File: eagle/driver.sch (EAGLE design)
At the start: 89 parts, among them IC1 XMEGA128A1, IC10 ST95P08M, IC11 ST95P08M, IC12 ST95P08M, IC13 ST95P08M, IC14 ST95P08M, IC15 ST95P08M, IC16 74AHC1G02DBV, IC17 74AHC1G02DBV, IC18 74AHC1G125DBV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

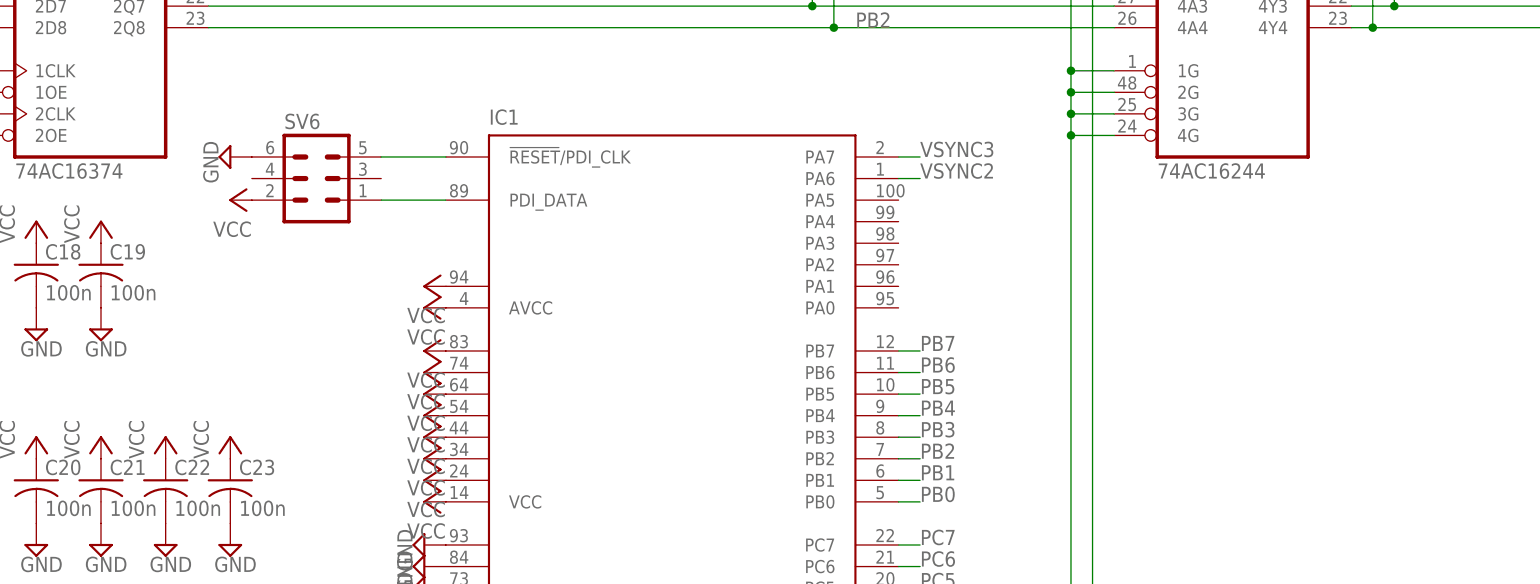
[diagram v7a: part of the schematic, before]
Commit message: add reset button and status leds
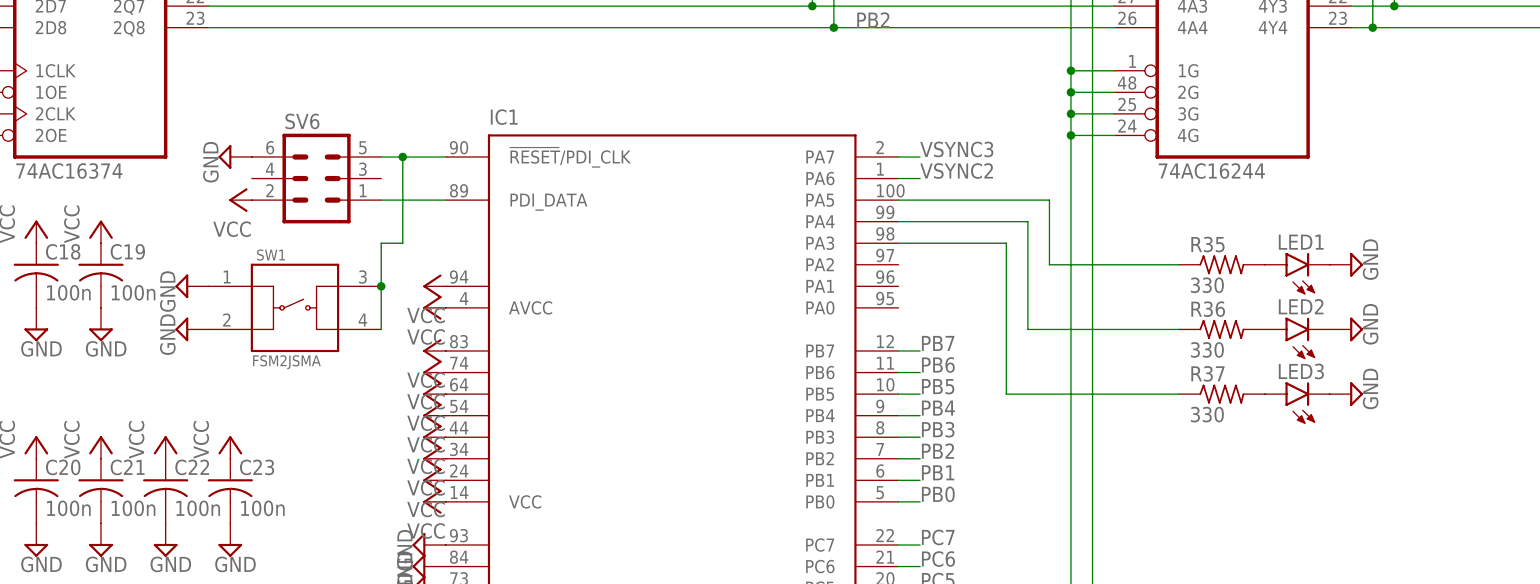
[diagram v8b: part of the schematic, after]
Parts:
- added LED1, LED2, LED3: (no value), led:LEDCHIPLED_0805
- added R35, R36, R37: 330, rcl:R-US_R0402
- added SW1: FSM2JSMA, Switch:FSM2JSMA
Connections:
- removed net N$88: IC1.!RESET!/PDI_CLK, SV6.5
- new net N$63: IC1.!RESET!/PDI_CLK, SV6.5, SW1.3, SW1.4
- new net N$66: LED3.A, R37.2
- new net N$67: LED2.A, R36.2
- new net N$69: LED1.A, R35.2
- new net N$71: IC1.PA5, R35.1
- new net N$73: IC1.PA4, R36.1
- new net N$75: IC1.PA3, R37.1
- net GND: now also LED1.C, LED2.C, LED3.C, SW1.1, SW1.2
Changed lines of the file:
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@@
 <layer number="132" name="bAdjust" color="7" fill="1" visible="yes" active="yes"/>
 <layer number="144" name="Drill_legend" color="7" fill="1" visible="yes" active="yes"/>
+<layer number="145" name="DrillLegend_01-16" color="2" fill="9" visible="no" active="yes"/>
+<layer number="146" name="DrillLegend_01-20" color="3" fill="9" visible="no" active="yes"/>
 <layer number="150" name="Notes" color="7" fill="1" visible="yes" active="yes"/>
 <layer number="151" name="HeatSink" color="7" fill="1" visible="yes" active="yes"/>
@@
 <part name="SUPPLY109" library="supply2" library_urn="urn:adsk.eagle:library:372" deviceset="GND" device=""/>
 <part name="SUPPLY110" library="supply2" library_urn="urn:adsk.eagle:library:372" deviceset="GND" device=""/>
+<part name="SW1" library="Switch" library_urn="urn:adsk.eagle:library:11396471" deviceset="FSM2JSMA" device="" package3d_urn="urn:adsk.eagle:package:12788212/3"/>
+<part name="SUPPLY111" library="supply2" library_urn="urn:adsk.eagle:library:372" deviceset="GND" device=""/>
+<part name="SUPPLY112" library="supply2" library_urn="urn:adsk.eagle:library:372" deviceset="GND" device=""/>
+<part name="R35" library="rcl" library_urn="urn:adsk.eagle:library:334" deviceset="R-US_" device="R0402" package3d_urn="urn:adsk.eagle:package:23547/3" value="330"/>
+<part name="R36" library="rcl" library_urn="urn:adsk.eagle:library:334" deviceset="R-US_" device="R0402" package3d_urn="urn:adsk.eagle:package:23547/3" value="330"/>
+<part name="R37" library="rcl" library_urn="urn:adsk.eagle:library:334" deviceset="R-US_" device="R0402" package3d_urn="urn:adsk.eagle:package:23547/3" value="330"/>
+<part name="LED1" library="led" library_urn="urn:adsk.eagle:library:259" deviceset="LED" device="CHIPLED_0805" package3d_urn="urn:adsk.eagle:package:15821/2"/>
+<part name="LED2" library="led" library_urn="urn:adsk.eagle:library:259" deviceset="LED" device="CHIPLED_0805" package3d_urn="urn:adsk.eagle:package:15821/2"/>
+<part name="LED3" library="led" library_urn="urn:adsk.eagle:library:259" deviceset="LED" device="CHIPLED_0805" package3d_urn="urn:adsk.eagle:package:15821/2"/>
+<part name="SUPPLY113" library="supply2" library_urn="urn:adsk.eagle:library:372" deviceset="GND" device=""/>
+<part name="SUPPLY114" library="supply2" library_urn="urn:adsk.eagle:library:372" deviceset="GND" device=""/>
+<part name="SUPPLY115" library="supply2" library_urn="urn:adsk.eagle:library:372" deviceset="GND" device=""/>
 </parts>
 <sheets>
@@
 <attribute name="VALUE" x="79.375" y="231.775" size="1.778" layer="96" rot="R90"/>
 </instance>
+<instance part="SW1" gate="G$1" x="127" y="144.78" smashed="yes">
+<attribute name="NAME" x="122.42458125" y="150.37218125" size="1.27095" layer="95"/>
+<attribute name="VALUE" x="121.910609375" y="137.90933125" size="1.27235" layer="96"/>
+</instance>
+<instance part="SUPPLY111" gate="GND" x="114.3" y="147.32" smashed="yes" rot="R270">
+<attribute name="VALUE" x="111.125" y="149.225" size="1.778" layer="96" rot="R270"/>
+</instance>
+<instance part="SUPPLY112" gate="GND" x="114.3" y="142.24" smashed="yes" rot="R270">
+<attribute name="VALUE" x="111.125" y="144.145" size="1.778" layer="96" rot="R270"/>
+</instance>
+<instance part="R35" gate="G$1" x="236.22" y="149.86" smashed="yes">
+<attribute name="NAME" x="232.41" y="151.3586" size="1.778" layer="95"/>
+<attribute name="VALUE" x="232.41" y="146.558" size="1.778" layer="96"/>
+</instance>
+<instance part="R36" gate="G$1" x="236.22" y="142.24" smashed="yes">
+<attribute name="NAME" x="232.41" y="143.7386" size="1.778" layer="95"/>
+<attribute name="VALUE" x="232.41" y="138.938" size="1.778" layer="96"/>
+</instance>
+<instance part="R37" gate="G$1" x="236.22" y="134.62" smashed="yes">
+<attribute name="NAME" x="232.41" y="136.1186" size="1.778" layer="95"/>
+<attribute name="VALUE" x="232.41" y="131.318" size="1.778" layer="96"/>
+</instance>
+<instance part="LED1" gate="G$1" x="243.84" y="149.86" smashed="yes" rot="R90">
+<attribute name="NAME" x="248.412" y="153.416" size="1.778" layer="95" rot="R180"/>
+<attribute name="VALUE" x="248.412" y="155.575" size="1.778" layer="96" rot="R180"/>
+</instance>
+<instance part="LED2" gate="G$1" x="243.84" y="142.24" smashed="yes" rot="R90">
+<attribute name="NAME" x="248.412" y="145.796" size="1.778" layer="95" rot="R180"/>
+<attribute name="VALUE" x="248.412" y="147.955" size="1.778" layer="96" rot="R180"/>
+</instance>
+<instance part="LED3" gate="G$1" x="243.84" y="134.62" smashed="yes" rot="R90">
+<attribute name="NAME" x="248.412" y="138.176" size="1.778" layer="95" rot="R180"/>
+<attribute name="VALUE" x="248.412" y="140.335" size="1.778" layer="96" rot="R180"/>
+</instance>
+<instance part="SUPPLY113" gate="GND" x="251.46" y="149.86" smashed="yes" rot="R90">
+<attribute name="VALUE" x="254.635" y="147.955" size="1.778" layer="96" rot="R90"/>
+</instance>
+<instance part="SUPPLY114" gate="GND" x="251.46" y="142.24" smashed="yes" rot="R90">
+<attribute name="VALUE" x="254.635" y="140.335" size="1.778" layer="96" rot="R90"/>
+</instance>
+<instance part="SUPPLY115" gate="GND" x="251.46" y="134.62" smashed="yes" rot="R90">
+<attribute name="VALUE" x="254.635" y="132.715" size="1.778" layer="96" rot="R90"/>
+</instance>
 </instances>
 <busses>
@@
 <junction x="73.66" y="233.68"/>
 </segment>
+<segment>
+<pinref part="SW1" gate="G$1" pin="1"/>
+<pinref part="SUPPLY111" gate="GND" pin="GND"/>
+</segment>
+<segment>
+<pinref part="SW1" gate="G$1" pin="2"/>
+<pinref part="SUPPLY112" gate="GND" pin="GND"/>
+</segment>
+<segment>
+<pinref part="LED1" gate="G$1" pin="C"/>
+<pinref part="SUPPLY113" gate="GND" pin="GND"/>
+</segment>
+<segment>
+<pinref part="LED2" gate="G$1" pin="C"/>
+<pinref part="SUPPLY114" gate="GND" pin="GND"/>
+</segment>
+<segment>
+<pinref part="LED3" gate="G$1" pin="C"/>
+<pinref part="SUPPLY115" gate="GND" pin="GND"/>
+</segment>
 </net>
 <net name="N$7" class="0">
@@
 </segment>
 </net>
-<net name="N$88" class="0">
-<segment>
-<pinref part="IC1" gate="G$1" pin="!RESET!/PDI_CLK"/>
-<pinref part="SV6" gate="1" pin="5"/>
-<wire x1="144.78" y1="162.56" x2="137.16" y2="162.56" width="0.1524" layer="91"/>
-</segment>
-</net>
 <net name="N$89" class="0">
 <segment>
@@
 </segment>
 </net>
+<net name="N$63" class="0">
+<segment>
+<pinref part="SW1" gate="G$1" pin="4"/>
+<pinref part="SW1" gate="G$1" pin="3"/>
+<wire x1="137.16" y1="142.24" x2="137.16" y2="147.32" width="0.1524" layer="91"/>
+<wire x1="137.16" y1="147.32" x2="137.16" y2="152.4" width="0.1524" layer="91"/>
+<junction x="137.16" y="147.32"/>
+<wire x1="137.16" y1="152.4" x2="139.7" y2="152.4" width="0.1524" layer="91"/>
+<pinref part="IC1" gate="G$1" pin="!RESET!/PDI_CLK"/>
+<pinref part="SV6" gate="1" pin="5"/>
+<wire x1="144.78" y1="162.56" x2="139.7" y2="162.56" width="0.1524" layer="91"/>
+<wire x1="139.7" y1="162.56" x2="137.16" y2="162.56" width="0.1524" layer="91"/>
+<wire x1="139.7" y1="152.4" x2="139.7" y2="162.56" width="0.1524" layer="91"/>
+<junction x="139.7" y="162.56"/>
+</segment>
+</net>
+<net name="N$66" class="0">
+<segment>
+<pinref part="R37" gate="G$1" pin="2"/>
+<pinref part="LED3" gate="G$1" pin="A"/>
+</segment>
+</net>
+<net name="N$67" class="0">
+<segment>
+<pinref part="R36" gate="G$1" pin="2"/>
+<pinref part="LED2" gate="G$1" pin="A"/>
+</segment>
+</net>
+<net name="N$69" class="0">
+<segment>
+<pinref part="R35" gate="G$1" pin="2"/>
+<pinref part="LED1" gate="G$1" pin="A"/>
+</segment>
+</net>
+<net name="N$71" class="0">
+<segment>
+<pinref part="IC1" gate="G$1" pin="PA5"/>
+<wire x1="198.12" y1="157.48" x2="215.9" y2="157.48" width="0.1524" layer="91"/>
+<wire x1="215.9" y1="157.48" x2="215.9" y2="149.86" width="0.1524" layer="91"/>
+<pinref part="R35" gate="G$1" pin="1"/>
+<wire x1="215.9" y1="149.86" x2="231.14" y2="149.86" width="0.1524" layer="91"/>
+</segment>
+</net>
+<net name="N$73" class="0">
+<segment>
+<pinref part="R36" gate="G$1" pin="1"/>
+<wire x1="231.14" y1="142.24" x2="213.36" y2="142.24" width="0.1524" layer="91"/>
+<wire x1="213.36" y1="142.24" x2="213.36" y2="154.94" width="0.1524" layer="91"/>
+<pinref part="IC1" gate="G$1" pin="PA4"/>
+<wire x1="213.36" y1="154.94" x2="198.12" y2="154.94" width="0.1524" layer="91"/>
+</segment>
+</net>
+<net name="N$75" class="0">
+<segment>
+<pinref part="IC1" gate="G$1" pin="PA3"/>
+<wire x1="198.12" y1="152.4" x2="210.82" y2="152.4" width="0.1524" layer="91"/>
+<wire x1="210.82" y1="152.4" x2="210.82" y2="134.62" width="0.1524" layer="91"/>
+<pinref part="R37" gate="G$1" pin="1"/>
+<wire x1="210.82" y1="134.62" x2="231.14" y2="134.62" width="0.1524" layer="91"/>
+</segment>
+</net>
